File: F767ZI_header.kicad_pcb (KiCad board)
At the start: 2 copper layers, 73 x 98.4 mm, 22 parts, among them J2 CAN1, J3 CAN2, J4 UART, J5 PowerBoard, J6 EMERSW_CON, J7 I2C1_default, J9 RESET_SW, SW1 SW_Push, U1 MCP2562-E-P, U2 MCP2562-E-P

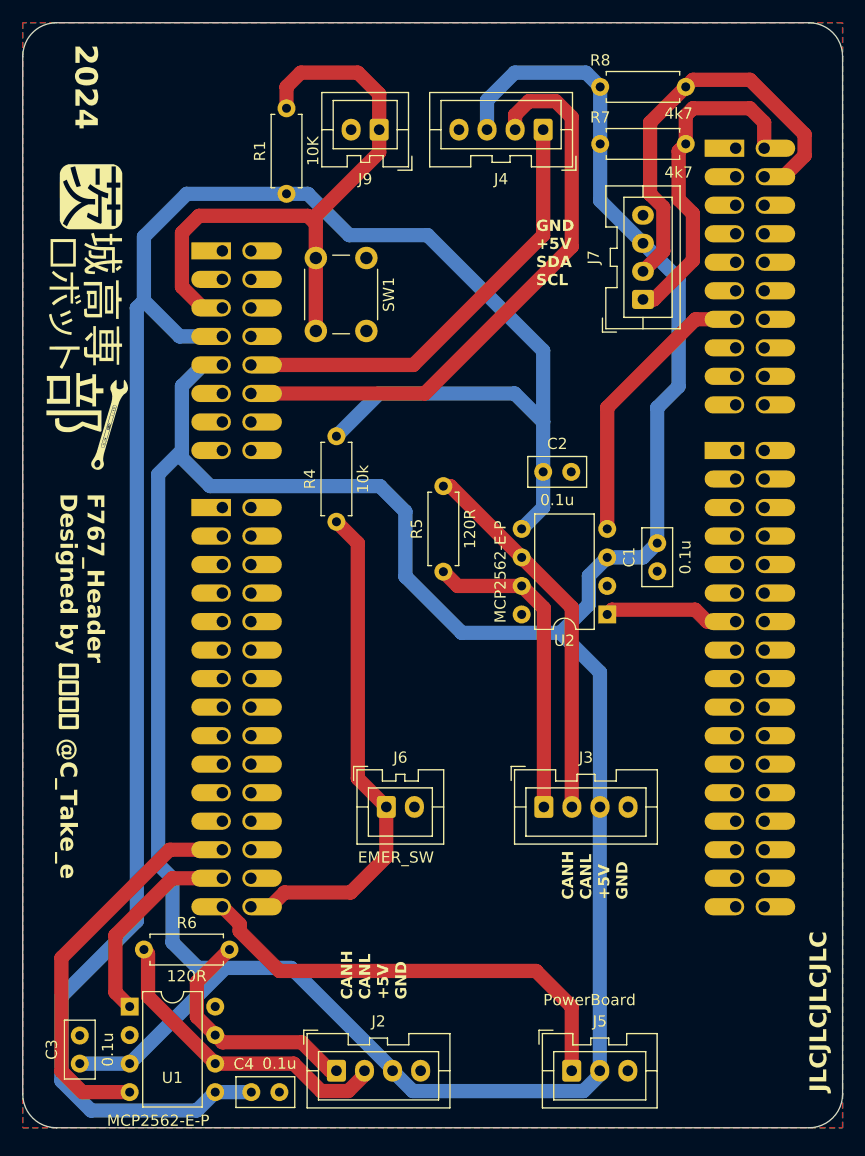
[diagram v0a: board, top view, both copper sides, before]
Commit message: PCB/SCH: EMER_SIGのピン変更、コネクタ再配置
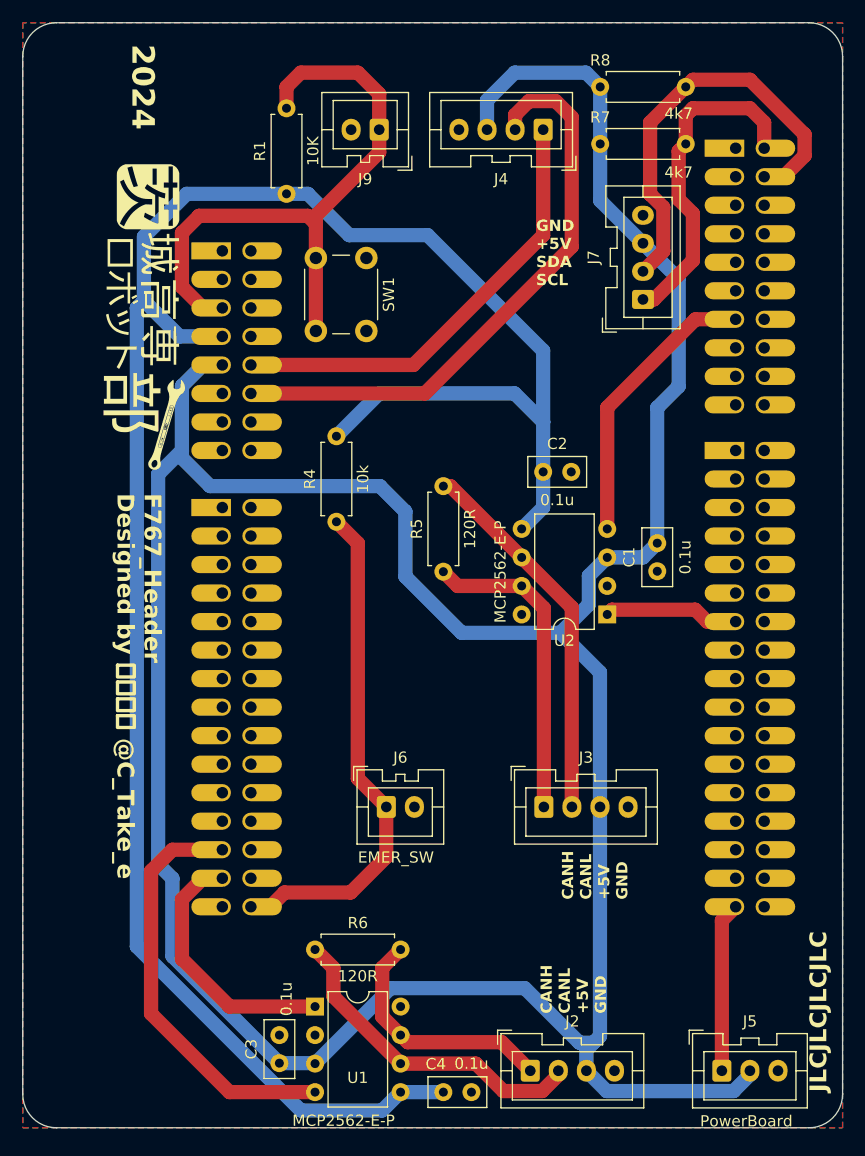
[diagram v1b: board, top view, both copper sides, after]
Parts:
- moved C3 17.8 mm to (177.2, 142.8)
- moved J2 17.3 mm to (199.5, 143.5)
- moved C4 17.1 mm to (191.8, 145.4)
- moved U1 16.5 mm to (180.3, 137.8)
- moved R6 15.2 mm to (188.0, 132.7)
- moved J5 13.4 mm to (216.6, 143.5)
- moved G*** 5.08 mm to (165.1, 76.8)
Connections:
- A1 pad CN10_33: unconnected-(A1D-D34/PE_0/TIMER_B_ETR-PadCN10_33) -> EMER_SIG
- A1 pad CN9_29: EMER_SIG -> unconnected-(A1C-D65/PG_0/IO-PadCN9_29)
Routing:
- net EMER_SIG: track 40.9 -> 15.1 mm
- net CAN1_TD: track 18.5 -> 23.3 mm
- net +5V: track 274.8 -> 278.0 mm
- net CAN1_RD: track 35.3 -> 37.3 mm
- net CAN1L: track 28.1 -> 29.3 mm
- net +3V3: track 185.9 -> 186.5 mm

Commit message: PCB: 部品密度こそ正義
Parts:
- moved J5 26.3 mm to (207.6, 118.7), turned to 180 degrees
- moved R6 23.9 mm to (194.9, 109.9)
- moved C4 23.0 mm to (197.5, 123.2), turned to 90 degrees
- moved U1 20.8 mm to (184.8, 117.5)
- moved C3 20.7 mm to (181.0, 122.5)
- moved J6 17.9 mm to (184.8, 102.2)
- moved J2 14.0 mm to (192.4, 131.4), turned to 180 degrees
- moved J3 12.8 mm to (206.4, 108.6), turned to 90 degrees
- moved R5 10.5 mm to (194.3, 88.9)
- moved U2 9.53 mm to (206.4, 93.3)
- moved C1 8.23 mm to (210.8, 88.3)
- moved C2 7.62 mm to (200.7, 82.5)
- moved J7 3.18 mm to (206.4, 74.8)
- moved R1 2.54 mm to (175.3, 57.8)
- moved J9 1.91 mm to (184.2, 59.7)
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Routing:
- net +5V: track 278.0 -> 200.7 mm
- net +3V3: track 186.5 -> 162.9 mm
- net CAN2_RD: track 25.5 -> 16.0 mm
- net CAN1_TD: track 23.3 -> 31.0 mm
- net CAN1H: track 21.8 -> 28.9 mm
- net EMER_SW: track 45.6 -> 40.7 mm
- net CAN2_TD: track 12.1 -> 16.4 mm
- net CAN1L: track 29.3 -> 26.8 mm
- net I2C1_SCL: track 29.7 -> 31.8 mm
- net UART_RX: track 53.0 -> 54.6 mm
- net CAN2H: track 28.0 -> 26.7 mm
- net UART_TX: track 40.2 -> 40.7 mm
- net NRST: track 56.9 -> 56.4 mm
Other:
- board size 73 x 98.4 mm -> 66 x 87 mm
- board text added: "GND +5V CANL CANH"
- board text removed: "CANH CANL +5V GND"
